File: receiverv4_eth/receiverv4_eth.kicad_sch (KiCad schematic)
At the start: 25 parts, among them J1 Raspberry_Pi_4, J2 SM04B-SRSS-TB, J3 S2B-PH-SM4-TB, U1 Teensy4.0, U2 AP63300WU-7_mod

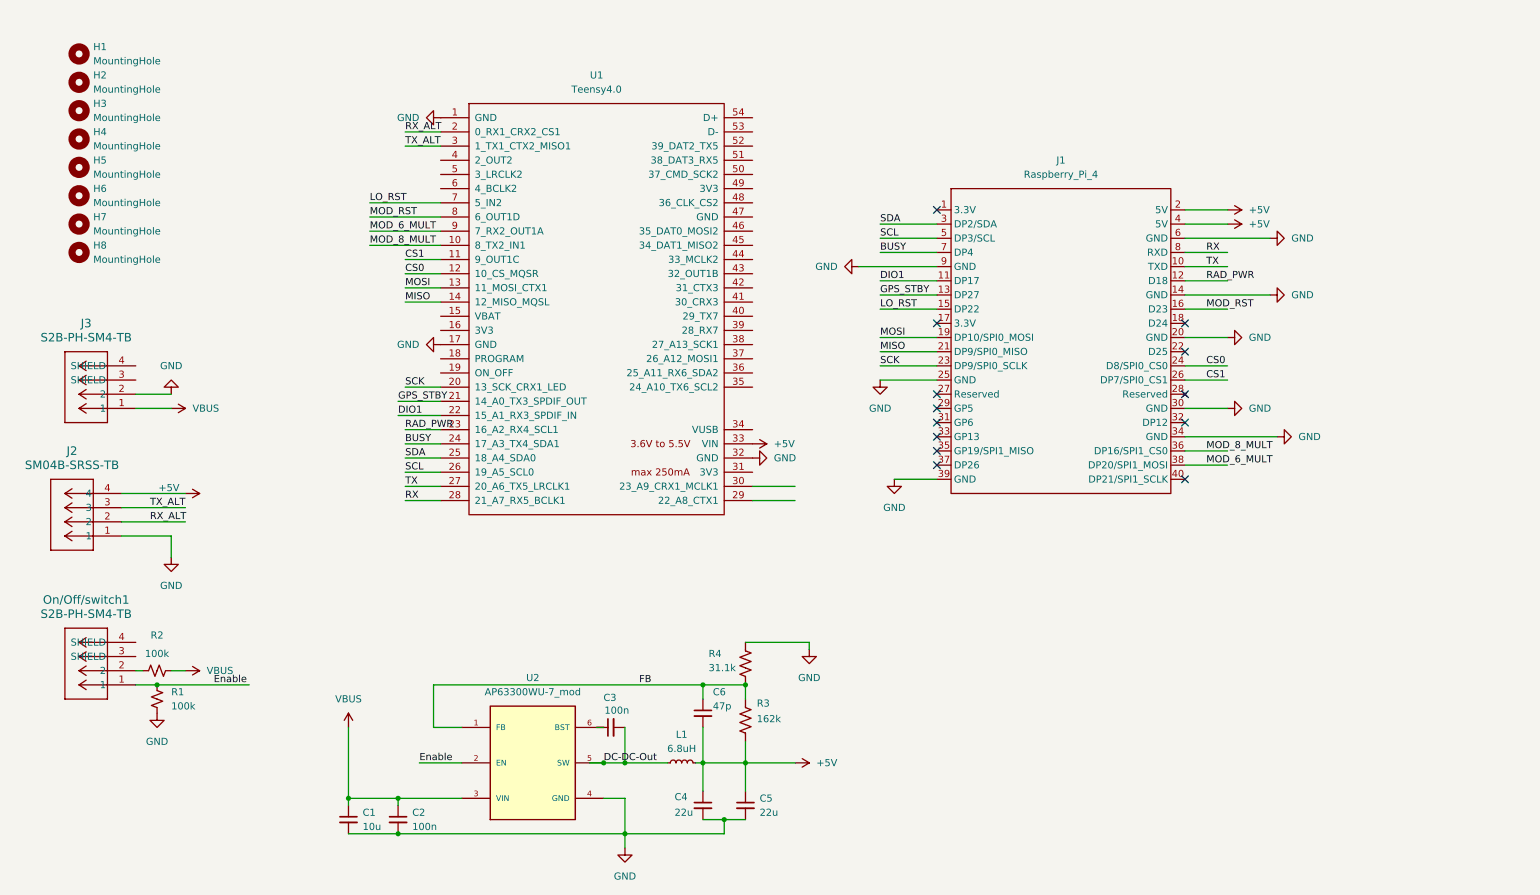
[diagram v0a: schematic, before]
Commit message: add teensy4.1 version of receiver
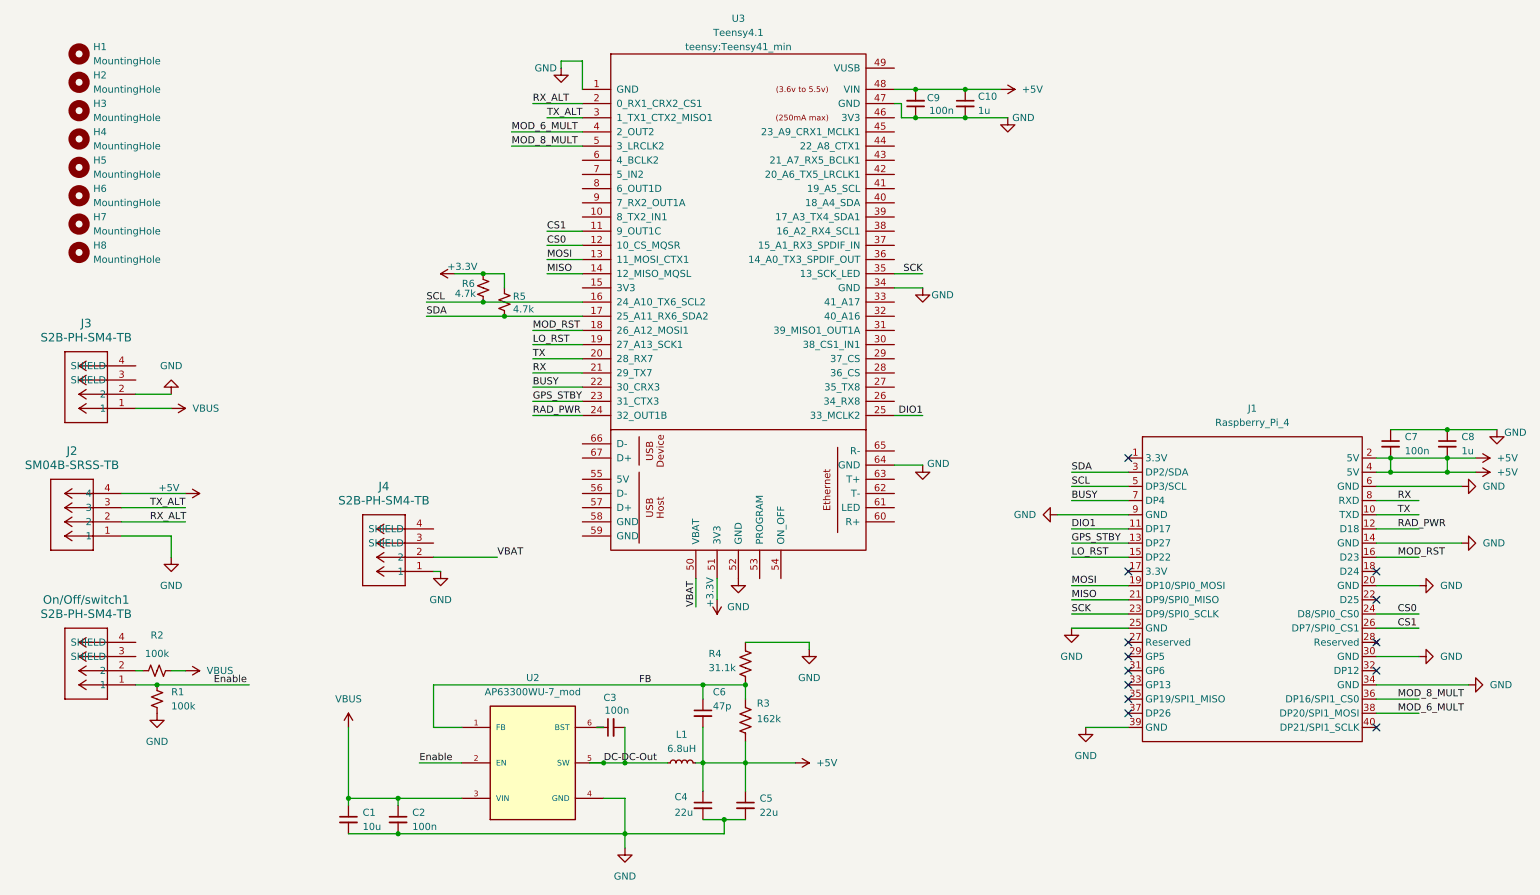
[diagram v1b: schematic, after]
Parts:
- removed U1: Teensy4.0, teensy:Teensy40_receiver, symbol teensy:Teensy4.0
- added C10, C8: 1u, Capacitor_SMD:C_0603_1608Metric_Pad1.08x0.95mm_HandSolder, symbol Device:C_Small
- added C7, C9: 100n, Capacitor_SMD:C_0402_1005Metric_Pad0.74x0.62mm_HandSolder, symbol Device:C_Small
- added J4: S2B-PH-SM4-TB, JST PH 2pin:CONN_S2B-PH-SM4-TB_JST, symbol JST PH 2pin:S2B-PH-SM4-TB
- added R5, R6: 4.7k, Resistor_SMD:R_0402_1005Metric, symbol Device:R_Small_US
- added U3: Teensy4.1, teensy:Teensy41_min, symbol teensy:Teensy4.1
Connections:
- net +5V: now also C10.1, C7.2, C8.2, C9.2, U3.48 (VIN)
- net BUSY: now also U3.22 (30_CRX3)
- net CS0: now also U3.12 (10_CS_MQSR)
- net CS1: now also U3.11 (9_OUT1C)
- net DIO1: now also U3.25 (33_MCLK2)
- net GND: now also C10.2, C7.1, C8.1, C9.1, J4.1, U3.1 (GND), U3.34 (GND), U3.47 (GND), U3.52 (GND), U3.64 (GND)
- net GPS_STBY: now also U3.23 (31_CTX3)
- net LO_RST: now also U3.19 (27_A13_SCK1)
- net MISO: now also U3.14 (12_MISO_MQSL)
- net MOD_6_MULT: now also U3.4 (2_OUT2)
- net MOD_8_MULT: now also U3.5 (3_LRCLK2)
- net MOD_RST: now also U3.18 (26_A12_MOSI1)
- net MOSI: now also U3.13 (11_MOSI_CTX1)
- net RAD_PWR: now also U3.24 (32_OUT1B)
- net RX: now also U3.21 (29_TX7)
- net RX_ALT: now also U3.2 (0_RX1_CRX2_CS1)
- net SCK: now also U3.35 (13_SCK_LED)
- net SCL: now also R6.2, U3.16 (24_A10_TX6_SCL2)
- net SDA: now also R5.2, U3.17 (25_A11_RX6_SDA2)
- net TX: now also U3.20 (28_RX7)
- net TX_ALT: now also U3.3 (1_TX1_CTX2_MISO1)
- new net +3.3V: R5.1, R6.1, U3.51 (3V3)
- new net VBAT: J4.2, U3.50 (VBAT)
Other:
- moved on the sheet: J1
